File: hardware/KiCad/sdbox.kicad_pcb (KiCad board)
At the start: 2 copper layers, 55 x 59 mm, 22 parts, among them J1 DB25_Male_MountingHoles, J2 Barrel_Jack, J5 Conn_01x01, J6 Conn_01x01, Q1 BC847BW, Q2 BC847BW, U1 Arduino_Nano_V3, U2 Micro_SD_Card_Module, U3 PVG612S

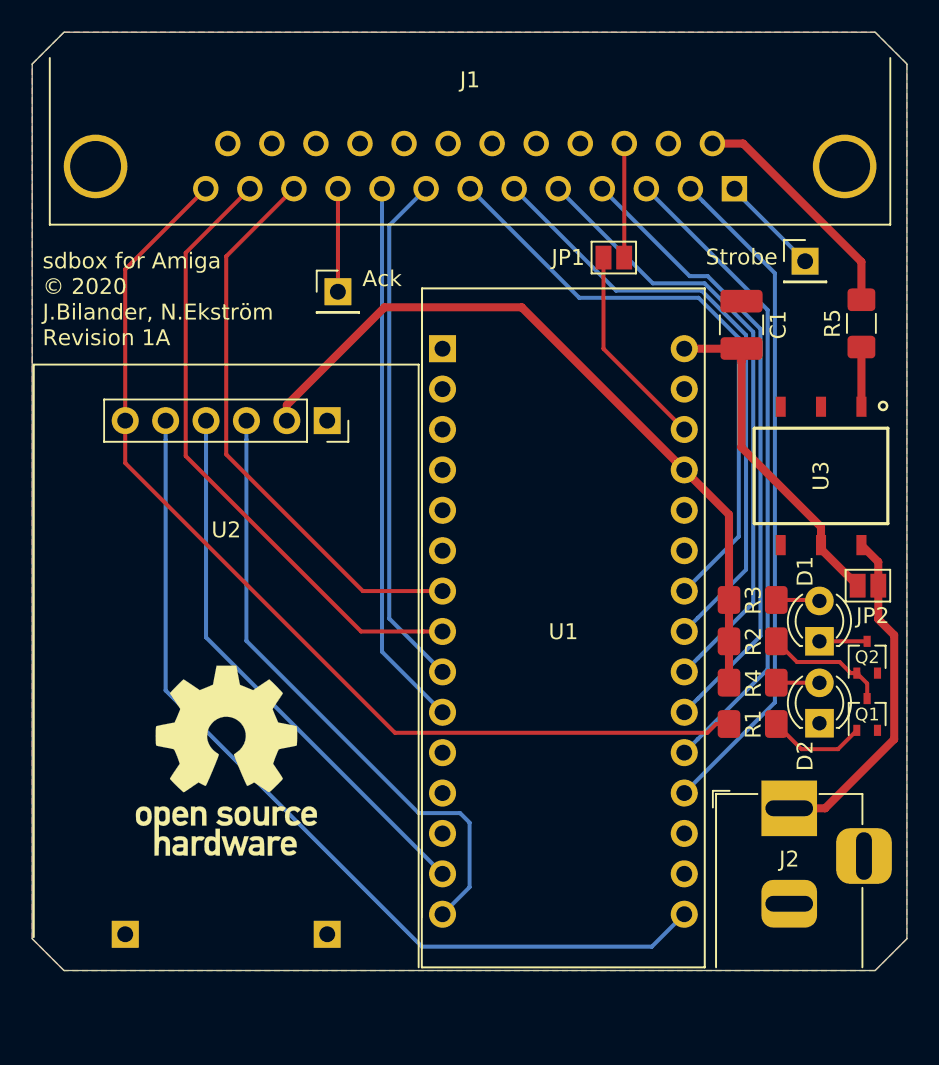
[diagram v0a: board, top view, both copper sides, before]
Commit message: Remove barrel jack, simplify power circuit, use SMD leds, improve 3D model
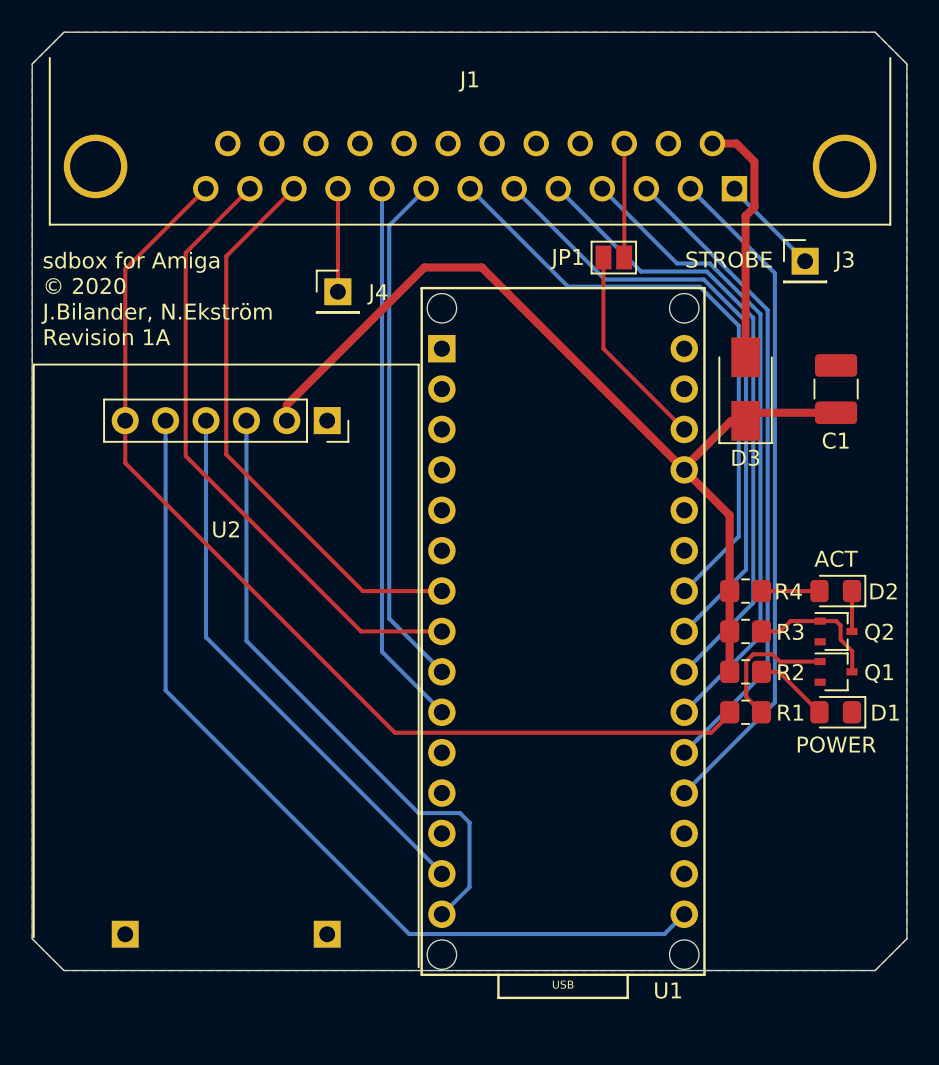
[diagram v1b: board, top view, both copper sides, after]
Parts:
- removed J2: Barrel_Jack, Connector_BarrelJack:BarrelJack_Horizontal
- removed JP2: SolderJumper_Open, Jumper:SolderJumper-2_P1.3mm_Open_Pad1.0x1.5mm
- removed R5: R_Small, Capacitor_SMD:C_1206_3216Metric_Pad1.42x1.75mm_HandSolder
- removed REF**: OSHW-Logo_11.4x12mm_SilkScreen, Symbol:OSHW-Logo_11.4x12mm_SilkScreen
- removed U3: PVG612S, Relay_SMD:SOIC254P978X443-6N
- added D3: 1n5819, Diode_SMD:D_SMA, F.Cu at (165.1, 107.4)
- D1: value Activity LED Indicator -> Power LED Indicator; footprint LED_THT:LED_D3.0mm -> LED_SMD:LED_0805_2012Metric_Pad1.15x1.40mm_HandSolder
- D2: value Power LED Indicator -> Activity LED Indicator; footprint LED_THT:LED_D3.0mm -> LED_SMD:LED_0805_2012Metric_Pad1.15x1.40mm_HandSolder
- J1: value DB25_Male_MountingHoles -> TO_PARALLEL_PORT
- R1, R2, R3, R4: footprint Resistor_SMD:R_1206_3216Metric_Pad1.42x1.75mm_HandSolder -> Resistor_SMD:R_0805_2012Metric_Pad1.20x1.40mm_HandSolder
- U1: footprint Arduino:Arduino_Nano_V3_Schield -> Arduino:Arduino_Nano_Socket
- U2: footprint Connector_PinSocket_2.54mm:PinSocket_1x06_P2.54mm_Vertical -> SDBox:MicroSDModule
- moved U1 21.6 mm to (153.6, 144.3)
- moved D2 8.37 mm to (170.7, 120.1), turned to 180 degrees
- moved C1 7.19 mm to (170.7, 107.4)
- moved R4 5.78 mm to (165.1, 120.1), turned to 180 degrees
- moved D1 4.58 mm to (170.7, 127.8), turned to 180 degrees
- moved Q1 3.32 mm to (170.7, 125.2), turned to 0 degrees
- moved Q2 2.54 mm to (170.7, 122.7), turned to 0 degrees
- moved R3 2.03 mm to (165.1, 122.7), turned to 0 degrees
- moved R2 1.97 mm to (165.1, 125.2)
- moved R1 0.86 mm to (165.1, 127.8)
- renumbered Strobe to J3, Ack to J4
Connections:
- C1 pad 2: Net-(C1-Pad2) -> 5V
- D1 pad 1: Net-(D1-Pad1) -> GND
- D2 pad 1: GND -> Net-(D2-Pad1)
- J1 pad 0: (no net) -> GND
- Q2 pad 3: Net-(D1-Pad1) -> Net-(D2-Pad1)
- R2 pad 2: Net-(Q1-Pad3) -> Net-(D1-Pad2)
- R3 pad 1: Net-(D1-Pad2) -> 5V
- R3 pad 2: 5V -> Net-(Q1-Pad3)
- R4 pad 1: 5V -> Net-(D2-Pad2)
- R4 pad 2: Net-(D2-Pad2) -> 5V
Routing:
- net Net-(C1-Pad2): track 21.5 -> 0.00 mm
- net VCC_7-12V: track 21.5 -> 0.00 mm
- net 5V: track 47.3 -> 59.8 mm
- net Net-(R5-Pad1): track 3.75 -> 0.00 mm
- net Net-(D1-Pad1): track 3.10 -> 0.00 mm
- net Net-(D2-Pad1): track 0.00 -> 2.54 mm
- net Net-(Q1-Pad1): track 6.21 -> 8.62 mm
- net Net-(D1-Pad2): track 2.74 -> 4.70 mm
- net Net-(Q1-Pad3): track 7.86 -> 8.79 mm
- net Net-(D2-Pad2): track 2.72 -> 3.64 mm
- net Amiga5V: track 14.8 -> 15.6 mm
- net SCK: track 57.1 -> 56.4 mm
- net D2: track 39.7 -> 40.2 mm
- net D3: track 39.2 -> 39.7 mm
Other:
- net class Default: trace_width 0.25 -> 0.254; via_dia 0.8 -> 0.6
- net class Power added: clearance 0.2, trace_width 0.508, via_dia 0.8, via_drill 0.6
- board text added: "ACT"
- board text added: "POWER"
- board text added: "STROBE"

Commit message: Switch connector to edge-mount
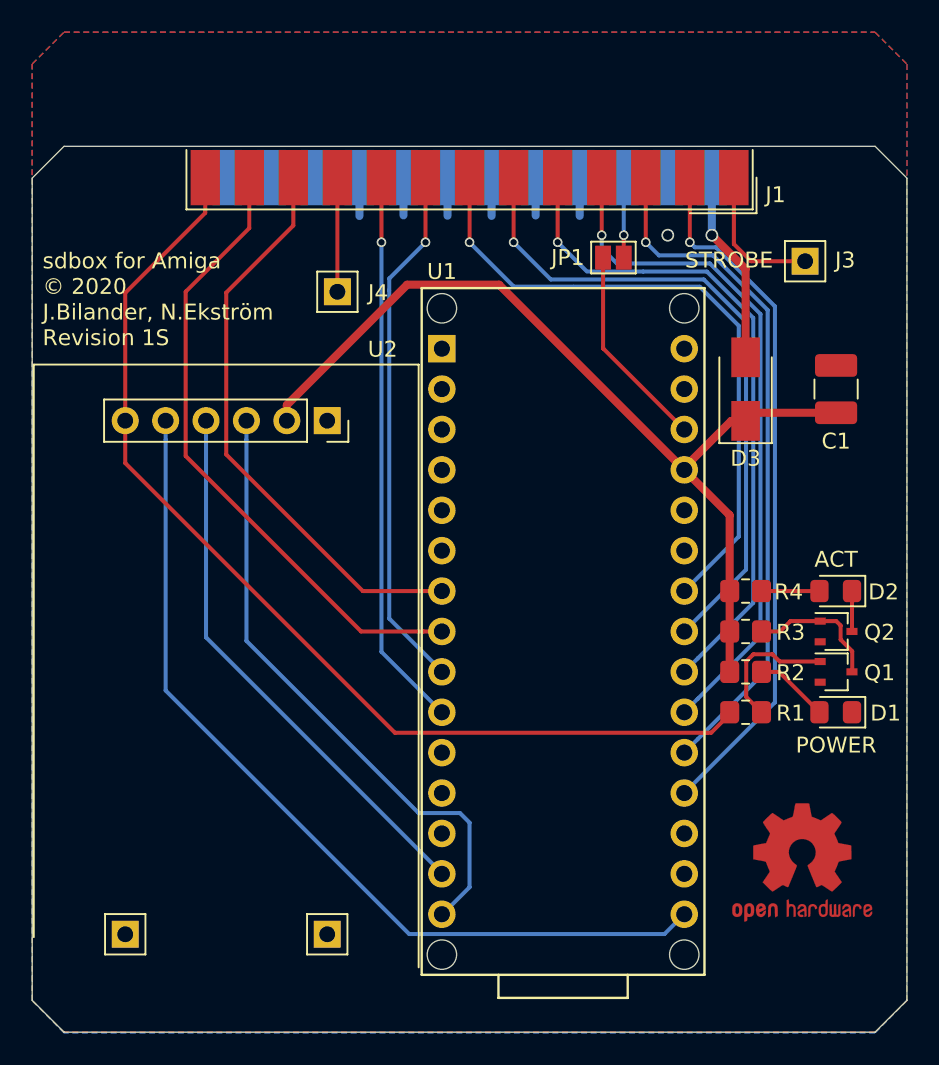
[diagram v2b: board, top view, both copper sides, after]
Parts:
- added V0: Void, Symbol:OSHW-Logo2_9.8x8mm_Copper, F.Cu at (168.6, 137.2)
- C1: value C_Small -> 100u
- J1: footprint Connector_Dsub:DSUB-25_Male_Horizontal_P2.77x2.84mm_EdgePinOffset4.94mm_Housed_MountingHolesOffset7.48mm -> Connector_Dsub:DSUB-25_Male_EdgeMount_P2.77mm
- J3, J4: footprint Connector_PinHeader_2.54mm:PinHeader_1x01_P2.54mm_Vertical -> SDBox:PinHeader_1x01_P2.54mm_Vertical
- J5, J6: footprint Connector_PinSocket_2.54mm:PinSocket_1x01_P2.54mm_Vertical -> SDBox:PinHeader_1x01_P2.54mm_Vertical
- R1, R3: value R_Small -> 4.7k
- R2, R4: value R_Small -> 120
- moved J1 16.7 mm to (147.7, 94.1)
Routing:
- net GND: track 0.00 -> 14.4 mm, vias 0 -> 1
- net Amiga5V: track 15.6 -> 12.2 mm, vias 0 -> 1
- net D2: track 40.2 -> 43.2 mm, vias 0 -> 1
- net D1: track 40.8 -> 43.5 mm, vias 0 -> 1
- net D4: track 39.1 -> 41.8 mm, vias 0 -> 1
- net D5: track 38.6 -> 41.3 mm, vias 0 -> 1
- net STROBE: track 6.41 -> 9.10 mm
- net D3: track 39.7 -> 42.3 mm, vias 0 -> 1
- net RESET: track 7.17 -> 5.11 mm, vias 0 -> 1
- net D0: track 42.6 -> 44.1 mm, vias 0 -> 1
- net 5V: track 59.8 -> 58.9 mm
- net D7: track 34.5 -> 35.2 mm, vias 0 -> 1
- net ACK: track 6.48 -> 7.18 mm
- net SELECT: track 65.0 -> 65.7 mm
- net BUSY: track 35.6 -> 36.3 mm
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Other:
- board size 55 x 59 mm -> 55 x 55.7 mm
- board text added: "sdbox for Amiga © 2020 J.Bilander, N.Ekström Revision 1S"
- board text removed: "sdbox for Amiga © 2020 J.Bilander, N.Ekström Revision 1A"

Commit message: Add ACK label
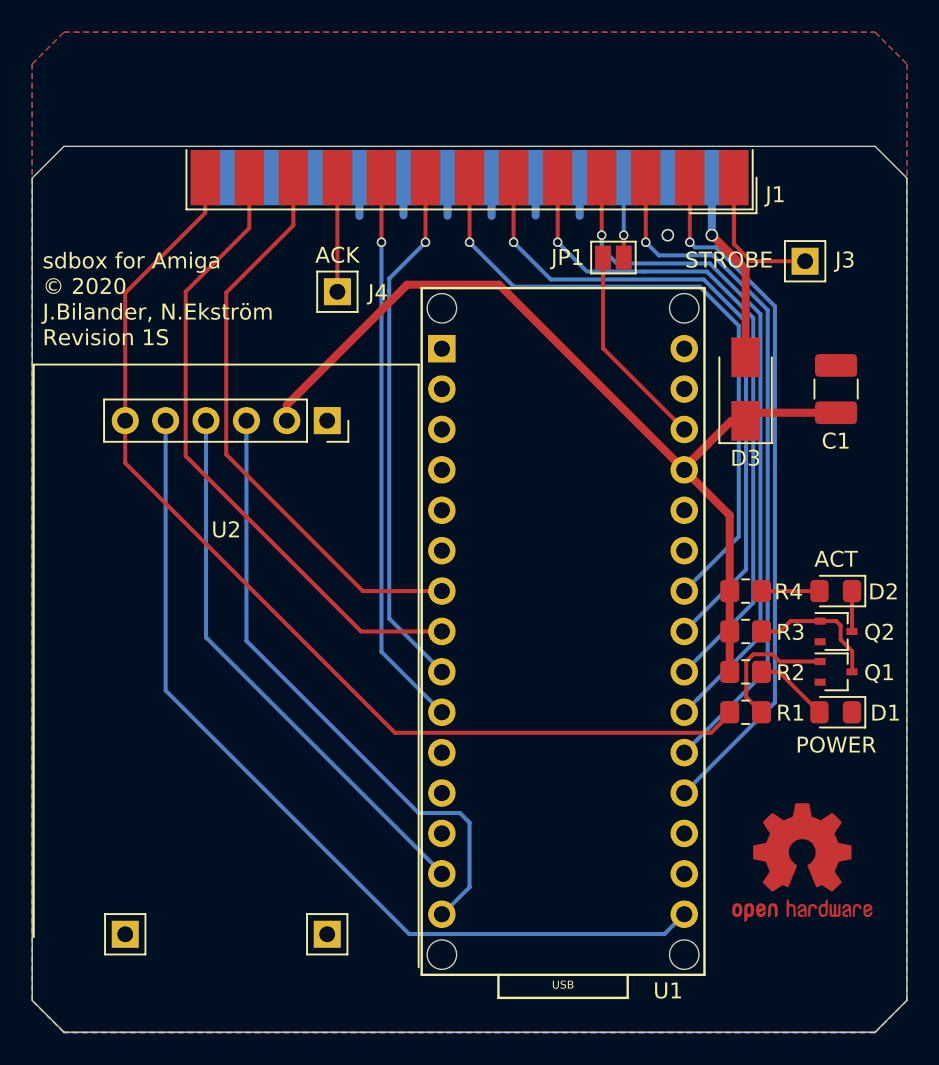
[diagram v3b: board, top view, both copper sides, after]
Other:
- board text added: "ACK"
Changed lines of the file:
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@@
   (general
     (thickness 1.6)
-    (drawings 12)
+    (drawings 13)
     (tracks 159)
     (zones 0)
@@
     (45 Margin user hide)
     (46 B.CrtYd user hide)
-    (47 F.CrtYd user)
+    (47 F.CrtYd user hide)
     (48 B.Fab user hide)
     (49 F.Fab user hide)
@@
     (at 153.58 144.27)
     (descr https://store.arduino.cc/arduino-nano)
-    (fp_text reference U1 (at -7.62 -44.2205) (layer F.SilkS)
+    (fp_text reference U1 (at 6.604 1.016) (layer F.SilkS)
       (effects (font (size 1 1) (thickness 0.15)))
     )
@@
       (effects (font (size 0.5 0.5) (thickness 0.075)))
     )
-    (fp_text user USB (at 0 0.635) (layer F.SilkS) hide
+    (fp_text user USB (at 0 0.635) (layer F.SilkS)
       (effects (font (size 0.5 0.5) (thickness 0.075)))
     )
@@
     (descr "Through hole straight socket strip, 1x06, 2.54mm pitch, single row (from Kicad 4.0.7), script generated")
     (tags "Through hole socket strip THT 1x06 2.54mm single row")
-    (fp_text reference U2 (at 9.8345 -4.461 180) (layer F.SilkS)
+    (fp_text reference U2 (at 0 6.9 180) (layer F.SilkS)
       (effects (font (size 1 1) (thickness 0.15)))
     )
@@
     (pad 1 thru_hole rect (at 0 0) (size 1.7 1.7) (drill 1) (layers *.Cu *.Mask)
       (net 25 STROBE))
+    (model ${KISYS3DMOD}/Connector_PinHeader_2.54mm.3dshapes/PinHeader_1x01_P2.54mm_Vertical.wrl
+      (at (xyz 0 0 0))
+      (scale (xyz 1 1 1))
+      (rotate (xyz 0 0 0))
+    )
   )
   (module SDBox:PinHeader_1x01_P2.54mm_Vertical (layer F.Cu)
@@
     (pad 1 thru_hole rect (at 0 0) (size 1.7 1.7) (drill 1) (layers *.Cu *.Mask)
       (net 24 ACK))
+    (model ${KISYS3DMOD}/Connector_PinHeader_2.54mm.3dshapes/PinHeader_1x01_P2.54mm_Vertical.wrl
+      (at (xyz 0 0 0))
+      (scale (xyz 1 1 1))
+      (rotate (xyz 0 0 0))
+    )
   )
   (module SDBox:PinHeader_1x01_P2.54mm_Vertical (layer F.Cu)
@@
     (pad 1 thru_hole rect (at 0 0) (size 1.7 1.7) (drill 1) (layers *.Cu *.Mask))
     (model ${KISYS3DMOD}/Connector_PinHeader_2.54mm.3dshapes/PinHeader_1x01_P2.54mm_Vertical.wrl
-      (offset (xyz 0 0 2.5))
-      (scale (xyz 1 1 1))
-      (rotate (xyz 180 0 0))
+      (at (xyz 0 0 0))
+      (scale (xyz 1 1 1))
+      (rotate (xyz 0 0 0))
     )
   )
@@
     (pad 1 thru_hole rect (at 0 0) (size 1.7 1.7) (drill 1) (layers *.Cu *.Mask))
     (model ${KISYS3DMOD}/Connector_PinHeader_2.54mm.3dshapes/PinHeader_1x01_P2.54mm_Vertical.wrl
-      (offset (xyz 0 0 2.5))
-      (scale (xyz 1 1 1))
-      (rotate (xyz 180 0 0))
-    )
+      (at (xyz 0 0 0))
+      (scale (xyz 1 1 1))
+      (rotate (xyz 0 0 0))
+    )
+  )
+  (gr_text ACK (at 139.39 99.0335) (layer F.SilkS)
+    (effects (font (size 1 1) (thickness 0.15)))
   )
   (gr_text POWER (at 170.746 129.831) (layer F.SilkS)
@@
     (connect_pads (clearance 0.1))
     (min_thickness 0.254)
-    (fill yes (arc_segments 32) (thermal_gap 0.254) (thermal_bridge_width 0.508))
+    (fill (arc_segments 32) (thermal_gap 0.254) (thermal_bridge_width 0.508))
     (polygon
       (pts
@@
     (connect_pads (clearance 0.1))
     (min_thickness 0.254)
-    (fill yes (arc_segments 32) (thermal_gap 0.254) (thermal_bridge_width 0.508))
+    (fill (arc_segments 32) (thermal_gap 0.254) (thermal_bridge_width 0.508))
     (polygon
       (pts
